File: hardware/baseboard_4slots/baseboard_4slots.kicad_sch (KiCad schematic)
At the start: 60 parts, among them J1 IO-Board_00, J10 Conn_01x04_Male, J11 Conn_01x04_Male, J12 Conn_01x04_Male, J13 Conn_01x04_Male, J14 Conn_01x04_Male, J2 IO-Board_01, J3 IO-Board_10, J4 IO-Board_11, J5 USB_B_Micro, J6 Conn_01x05: Adafruit 1833, J7 Screw_Terminal_01x04, J8 Conn_02x02_Odd_Even, J9 Conn_02x02_Odd_Even, U1 NRF24L01_Breakout, U2 Pico, U3 W5500_Mini

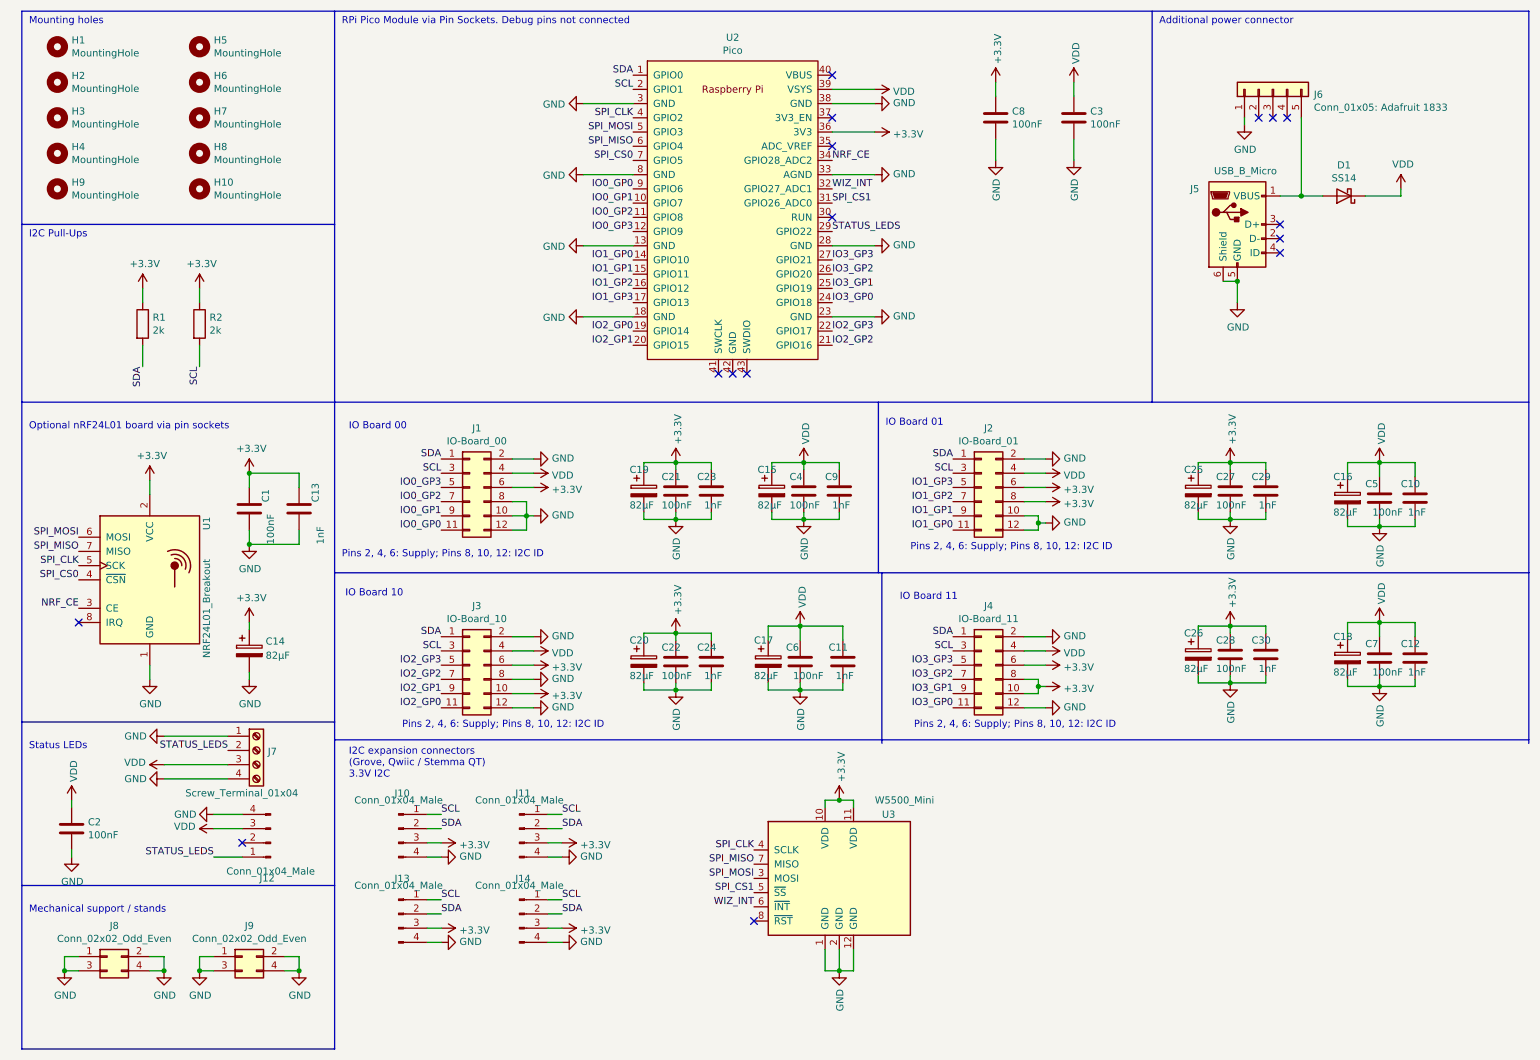
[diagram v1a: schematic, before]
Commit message: Connect the nRF24 to the now shared IRQ line and supress some ERC errors
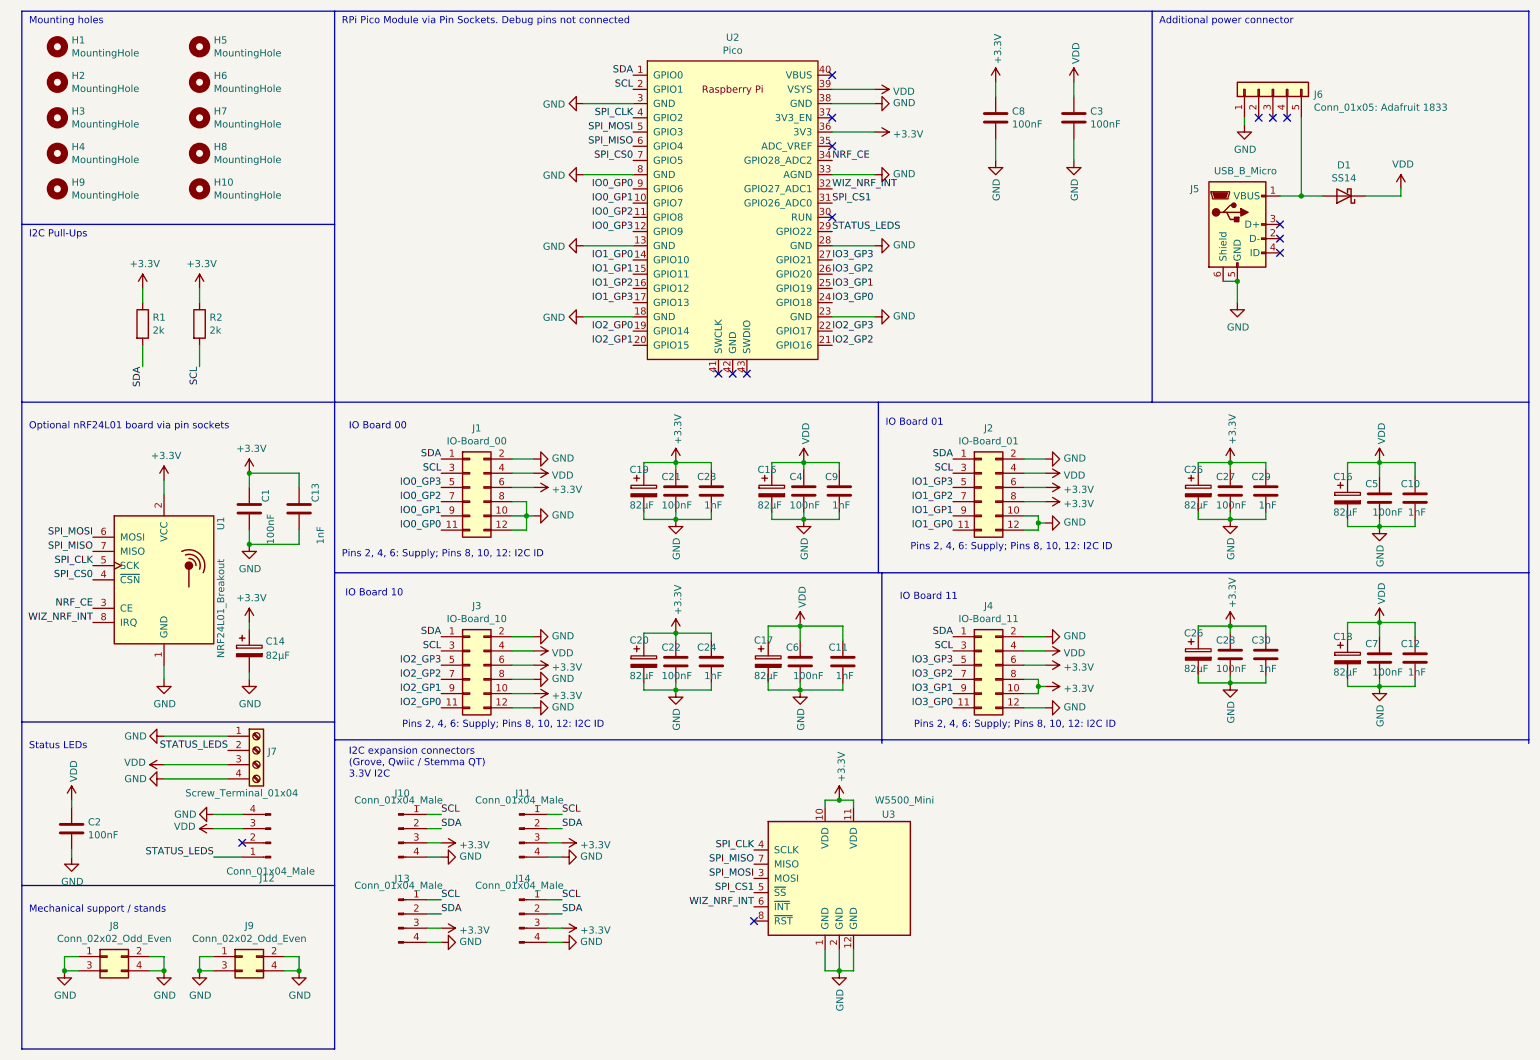
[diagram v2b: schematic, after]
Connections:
- net WIZ_INT is gone; now on net WIZ_NRF_INT: U2.32 (GPIO27_ADC1), U3.6 (~{INT})
- net WIZ_NRF_INT: now reaches U1.8 (IRQ)
- no-connect marks 16 -> 15
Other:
- moved on the sheet: U1
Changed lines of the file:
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@@
   )
   (no_connect (at 237.49 55.88))
-  (no_connect (at 22.86 121.92))
   (no_connect (at 157.48 24.13))
   (no_connect (at 157.48 36.83))
@@
     (stroke (width 0) (type default) (color 0 0 0 0))
   )
-  (wire (pts (xy 35.56 96.52) (xy 35.56 99.06))
+  (wire (pts (xy 38.1 96.52) (xy 38.1 99.06))
     (stroke (width 0) (type default) (color 0 0 0 0))
   )
@@
     (stroke (width 0) (type default) (color 0 0 0 0))
   )
-  (wire (pts (xy 35.56 129.54) (xy 35.56 132.08))
+  (wire (pts (xy 38.1 129.54) (xy 38.1 132.08))
     (stroke (width 0) (type default) (color 0 0 0 0))
   )
@@
     (effects (font (size 1.27 1.27)) (justify right bottom))
   )
-  (label "SPI_MISO" (at 22.86 109.22 180)
+  (label "SPI_MISO" (at 25.4 109.22 180)
     (effects (font (size 1.27 1.27)) (justify right bottom))
   )
@@
     (effects (font (size 1.27 1.27)) (justify right bottom))
   )
-  (label "WIZ_INT" (at 157.48 44.45 0)
+  (label "WIZ_NRF_INT" (at 157.48 44.45 0)
     (effects (font (size 1.27 1.27)) (justify left bottom))
   )
@@
     (effects (font (size 1.27 1.27)) (justify right bottom))
   )
-  (label "NRF_CE" (at 22.86 119.38 180)
+  (label "NRF_CE" (at 25.4 119.38 180)
     (effects (font (size 1.27 1.27)) (justify right bottom))
   )
@@
     (effects (font (size 1.27 1.27)) (justify right bottom))
   )
-  (label "WIZ_INT" (at 143.51 172.72 180)
+  (label "WIZ_NRF_INT" (at 143.51 172.72 180)
     (effects (font (size 1.27 1.27)) (justify right bottom))
   )
@@
     (effects (font (size 1.27 1.27)) (justify right bottom))
   )
-  (label "SPI_CS0" (at 22.86 114.3 180)
+  (label "SPI_CS0" (at 25.4 114.3 180)
     (effects (font (size 1.27 1.27)) (justify right bottom))
   )
@@
     (effects (font (size 1.27 1.27)) (justify right bottom))
   )
+  (label "WIZ_NRF_INT" (at 25.4 121.92 180)
+    (effects (font (size 1.27 1.27)) (justify right bottom))
+  )
   (label "IO2_GP3" (at 157.48 69.85 0)
     (effects (font (size 1.27 1.27)) (justify left bottom))
@@
     (effects (font (size 1.27 1.27)) (justify right bottom))
   )
-  (label "SPI_CLK" (at 22.86 111.76 180)
-    (effects (font (size 1.27 1.27)) (justify right bottom))
-  )
-  (label "SPI_MOSI" (at 22.86 106.68 180)
+  (label "SPI_CLK" (at 25.4 111.76 180)
+    (effects (font (size 1.27 1.27)) (justify right bottom))
+  )
+  (label "SPI_MOSI" (at 25.4 106.68 180)
     (effects (font (size 1.27 1.27)) (justify right bottom))
   )
@@
     (pin "1")
   )
-  (symbol (lib_id "RF:NRF24L01_Breakout") (at 35.56 114.3 0) (unit 1)
-    (in_bom yes) (on_board yes)
-    (property "Reference" "U1" (id 0) (at 45.72 105.41 90)
-      (effects (font (size 1.27 1.27)) (justify left))
-    )
-    (property "Value" "NRF24L01_Breakout" (id 1) (at 45.72 128.27 90)
-      (effects (font (size 1.27 1.27)) (justify left))
-    )
-    (property "Footprint" "RF_Module:nRF24L01_Breakout" (id 2) (at 39.37 99.06 0)
+  (symbol (lib_id "RF:NRF24L01_Breakout") (at 38.1 114.3 0) (unit 1)
+    (in_bom yes) (on_board yes)
+    (property "Reference" "U1" (id 0) (at 48.26 105.41 90)
+      (effects (font (size 1.27 1.27)) (justify left))
+    )
+    (property "Value" "NRF24L01_Breakout" (id 1) (at 48.26 128.27 90)
+      (effects (font (size 1.27 1.27)) (justify left))
+    )
+    (property "Footprint" "RF_Module:nRF24L01_Breakout" (id 2) (at 41.91 99.06 0)
       (effects (font (size 1.27 1.27) italic) (justify left) hide)
     )
-    (property "Datasheet" "http://www.nordicsemi.com/eng/content/download/2730/34105/file/nRF24L01_Product_Specification_v2_0.pdf" (id 3) (at 35.56 116.84 0)
+    (property "Datasheet" "http://www.nordicsemi.com/eng/content/download/2730/34105/file/nRF24L01_Product_Specification_v2_0.pdf" (id 3) (at 38.1 116.84 0)
       (effects (font (size 1.27 1.27)) hide)
     )
@@
     (pin "8")
   )
-  (symbol (lib_id "power:GND") (at 35.56 132.08 0) (unit 1)
-    (in_bom yes) (on_board yes)
-    (property "Reference" "#PWR04" (id 0) (at 35.56 138.43 0)
-      (effects (font (size 1.27 1.27)) hide)
-    )
-    (property "Value" "GND" (id 1) (at 35.687 136.4742 0))
-    (property "Footprint" "" (id 2) (at 35.56 132.08 0)
-      (effects (font (size 1.27 1.27)) hide)
-    )
-    (property "Datasheet" "" (id 3) (at 35.56 132.08 0)
-      (effects (font (size 1.27 1.27)) hide)
-    )
-    (pin "1")
-  )
-  (symbol (lib_id "power:+3.3V") (at 35.56 96.52 0) (unit 1)
-    (in_bom yes) (on_board yes)
-    (property "Reference" "#PWR03" (id 0) (at 35.56 100.33 0)
-      (effects (font (size 1.27 1.27)) hide)
-    )
-    (property "Value" "+3.3V" (id 1) (at 35.941 92.1258 0))
-    (property "Footprint" "" (id 2) (at 35.56 96.52 0)
-      (effects (font (size 1.27 1.27)) hide)
-    )
-    (property "Datasheet" "" (id 3) (at 35.56 96.52 0)
-      (effects (font (size 1.27 1.27)) hide)
-    )
+  (symbol (lib_id "power:GND") (at 38.1 132.08 0) (unit 1)
+    (in_bom yes) (on_board yes)
+    (property "Reference" "#PWR04" (id 0) (at 38.1 138.43 0)
+      (effects (font (size 1.27 1.27)) hide)
+    )
+    (property "Value" "GND" (id 1) (at 38.227 136.4742 0))
+    (property "Footprint" "" (id 2) (at 38.1 132.08 0)
+      (effects (font (size 1.27 1.27)) hide)
+    )
+    (property "Datasheet" "" (id 3) (at 38.1 132.08 0)
+      (effects (font (size 1.27 1.27)) hide)
+    )
+    (pin "1")
+  )
+  (symbol (lib_id "power:+3.3V") (at 38.1 96.52 0) (unit 1)
+    (in_bom yes) (on_board yes)
+    (property "Reference" "#PWR03" (id 0) (at 38.1 100.33 0)
+      (effects (font (size 1.27 1.27)) hide)
+    )
+    (property "Value" "+3.3V" (id 1) (at 38.481 92.1258 0))
+    (property "Footprint" "" (id 2) (at 38.1 96.52 0)
+      (effects (font (size 1.27 1.27)) hide)
+    )
+    (property "Datasheet" "" (id 3) (at 38.1 96.52 0)
+      (effects (font (size 1.27 1.27)) hide)
+    )

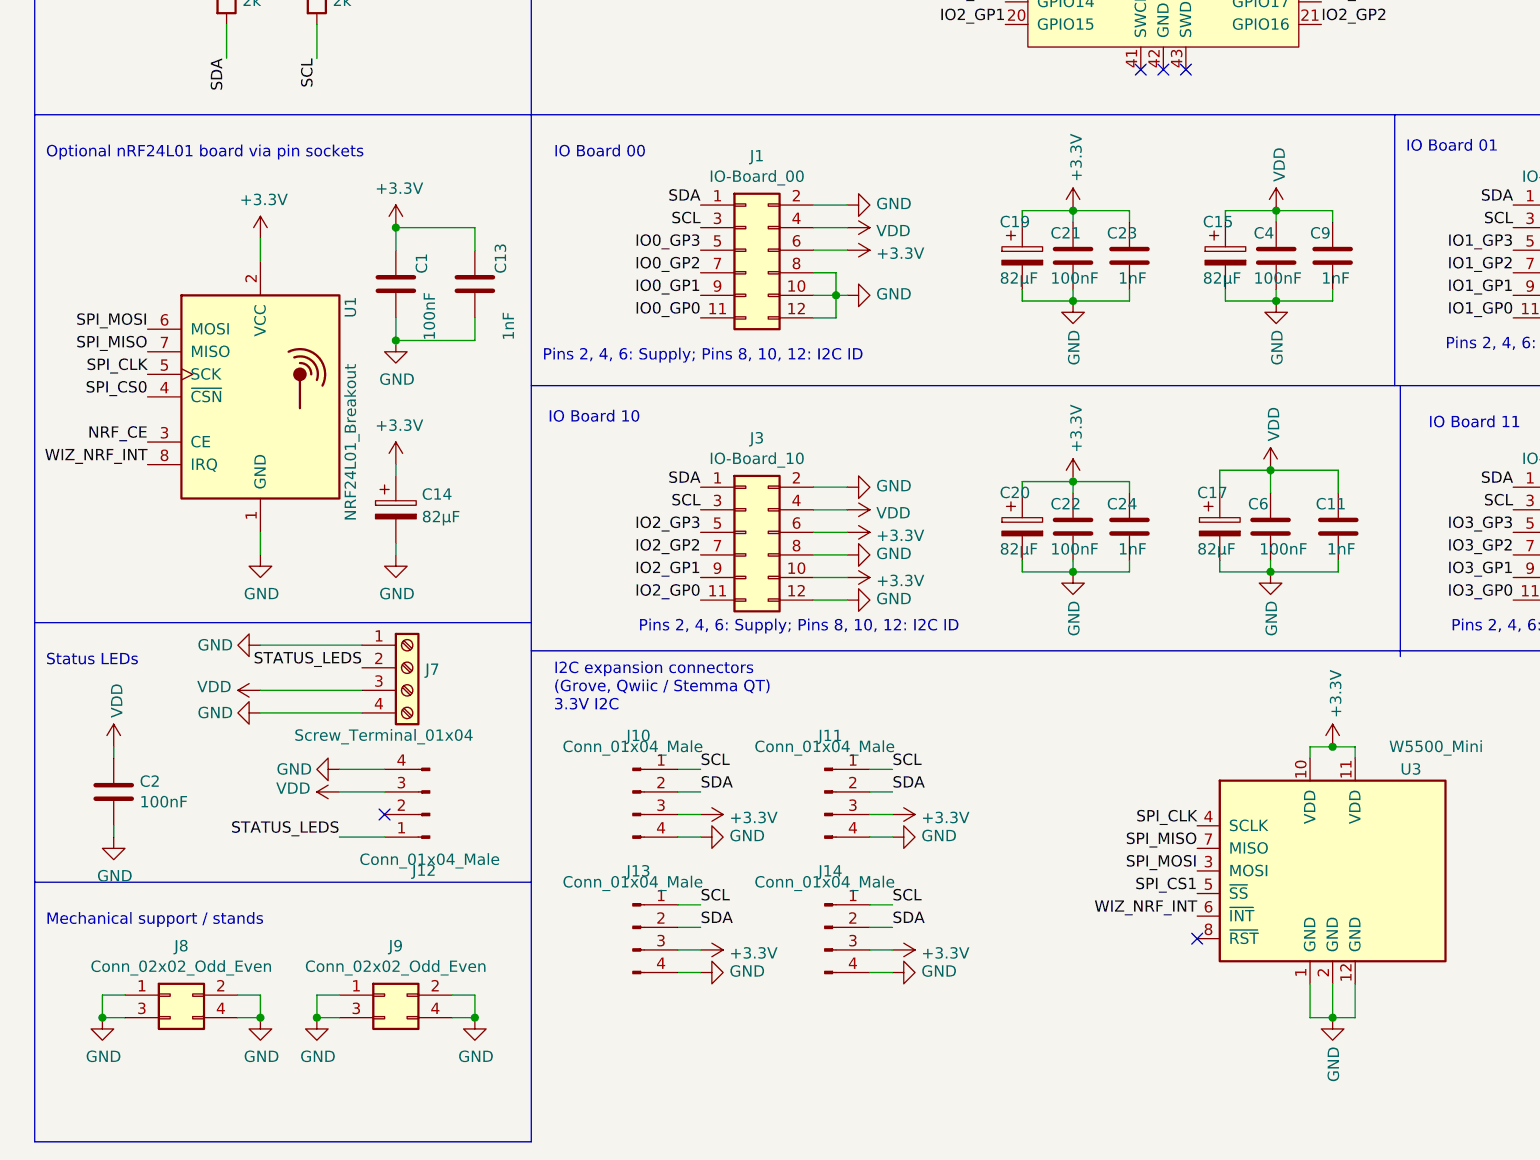
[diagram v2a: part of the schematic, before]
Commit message: Update W5500_Mini footprint and minor fixes on the baseboard
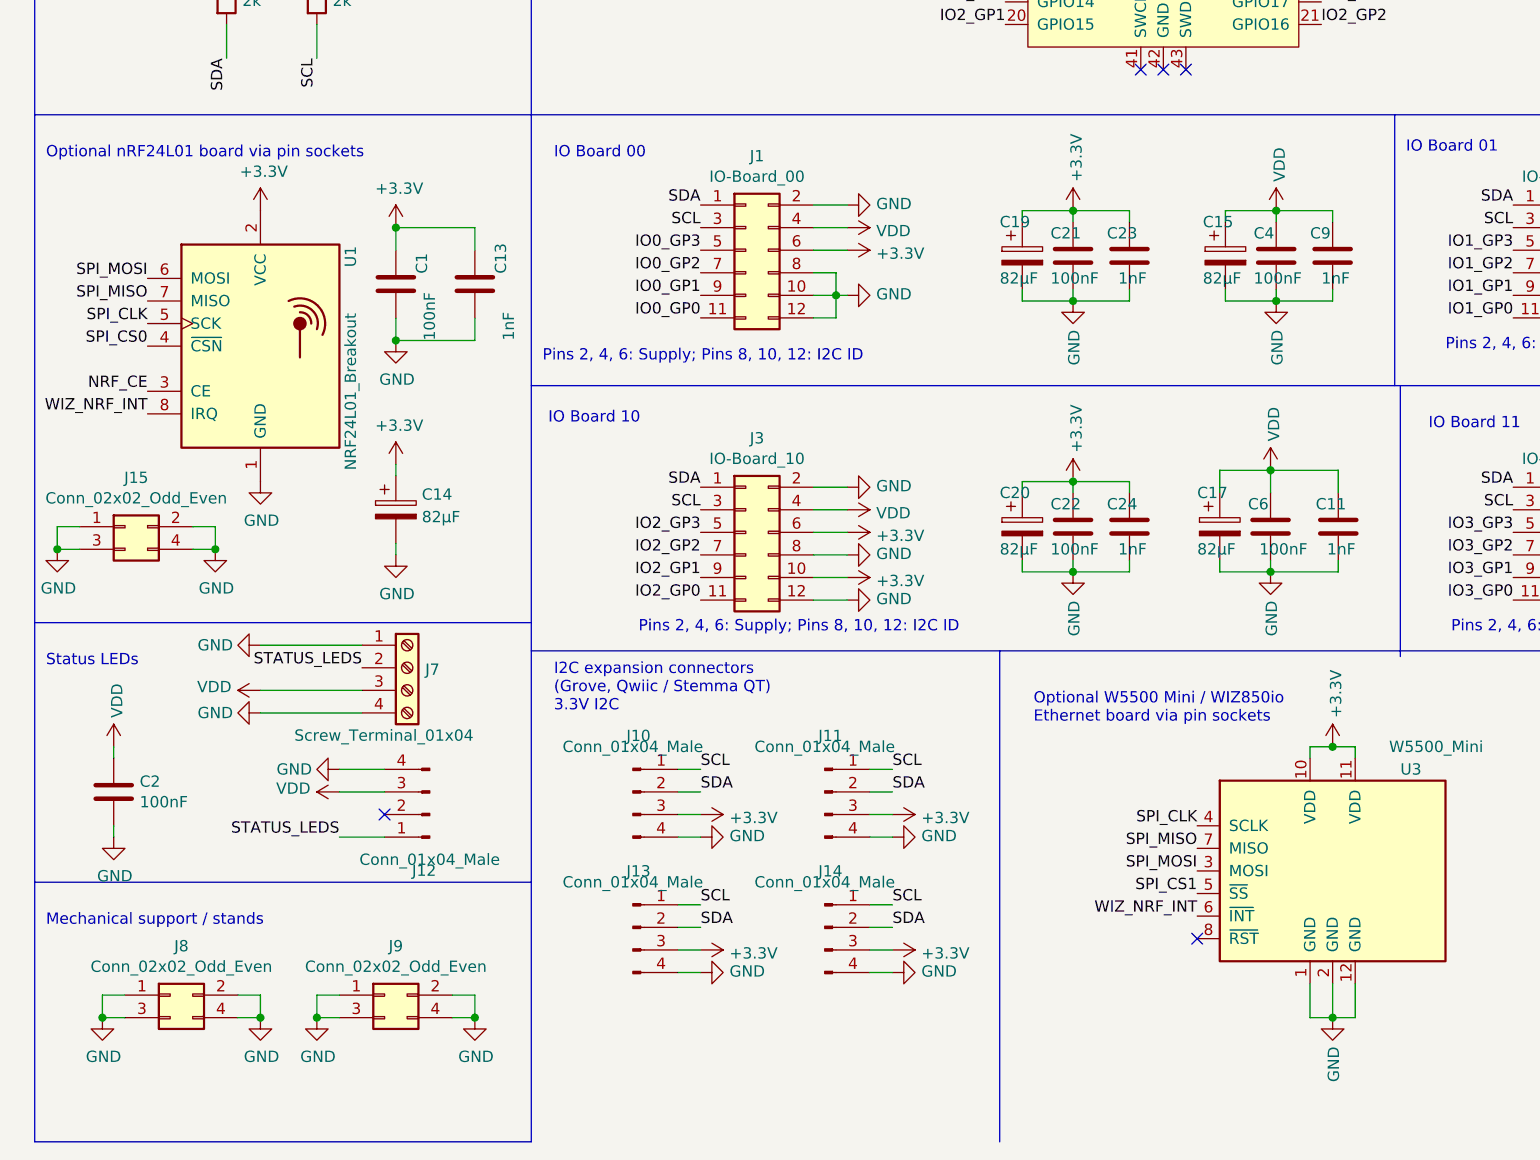
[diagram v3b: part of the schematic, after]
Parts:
- added J15: Conn_02x02_Odd_Even, Connector_PinSocket_2.54mm:PinSocket_2x02_P2.54mm_Vertical, symbol Connector_Generic:Conn_02x02_Odd_Even
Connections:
- net GND: now also J15.1 (Pin_1), J15.2 (Pin_2), J15.3 (Pin_3), J15.4 (Pin_4)
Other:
- note added: "Optional W5500 Mini / WIZ850io Ethernet board via pin sockets"
- moved on the sheet: U1

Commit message: Hardware: Add missing LCSC references for some caps
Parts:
- C23, C24, C29, C30, C9: LCSC (none) -> C1588
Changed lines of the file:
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@@
+      (effects (font (size 1.27 1.27)) hide)
+    )
+    (property "LCSC" "C1588" (id 4) (at 158.75 98.425 0)
       (effects (font (size 1.27 1.27)) hide)
     )
@@
       (effects (font (size 1.27 1.27)) hide)
     )
+    (property "LCSC" "C1588" (id 4) (at 234.95 127.635 0)
+      (effects (font (size 1.27 1.27)) hide)
+    )
     (pin "1")
     (pin "2")
@@
     )
     (property "Datasheet" "~" (id 3) (at 135.89 128.905 0)
+      (effects (font (size 1.27 1.27)) hide)
+    )
+    (property "LCSC" "C1588" (id 4) (at 135.89 128.905 0)
       (effects (font (size 1.27 1.27)) hide)
     )
@@
       (effects (font (size 1.27 1.27)) hide)
     )
+    (property "LCSC" "C1588" (id 4) (at 234.95 98.425 0)
+      (effects (font (size 1.27 1.27)) hide)
+    )
     (pin "1")
     (pin "2")
@@
       (effects (font (size 1.27 1.27)) hide)
     )
+    (property "LCSC" "C1588" (id 4) (at 135.89 98.425 0)
+      (effects (font (size 1.27 1.27)) hide)
+    )
